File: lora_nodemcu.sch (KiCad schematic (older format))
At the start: 12 parts, among them U1 RFM95, U2 LM1117-3.3, U3 WeMos_mini

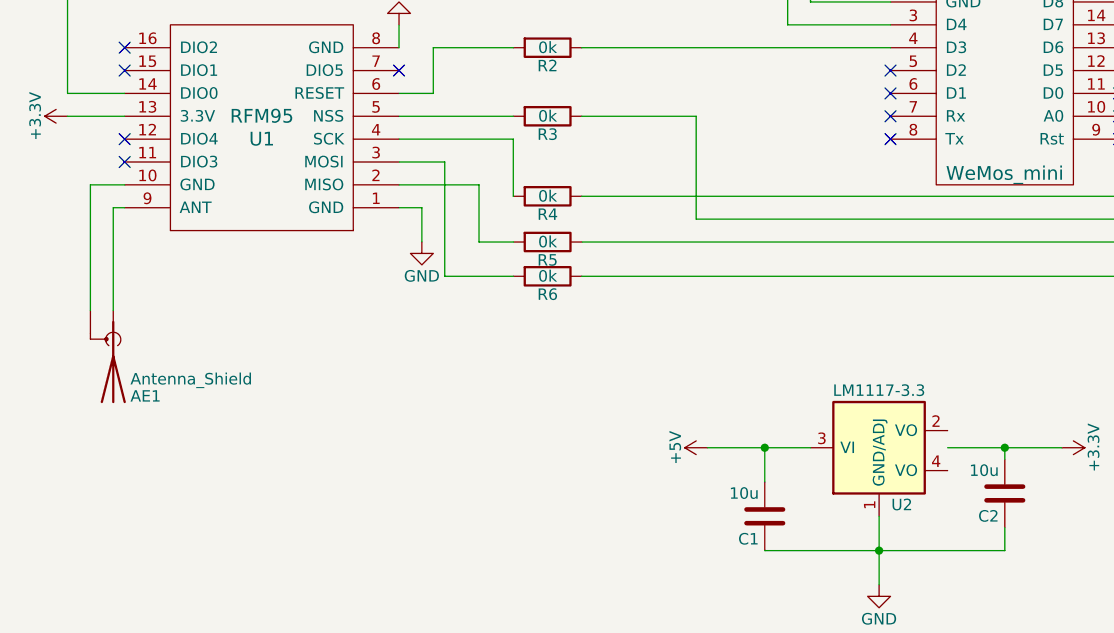
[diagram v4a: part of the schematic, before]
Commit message: fixed traces, added 3.3v power management
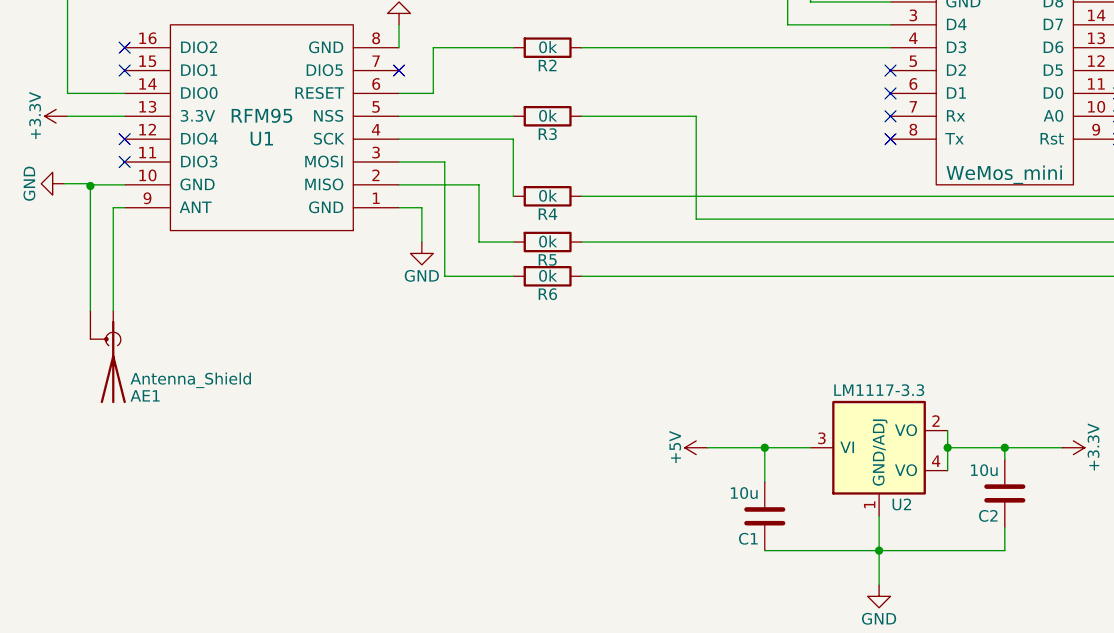
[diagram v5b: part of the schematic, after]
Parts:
- U2: footprint (none) -> TO_SOT_Packages_SMD:SOT-223
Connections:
- net +3V3: now also U2.2 (VO), U2.4 (VO)
- net GND: now also AE1.2 (Shield), U1.10 (GND)
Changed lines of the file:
@@
 LIBS:valves
 LIBS:rfm95
-LIBS:disaster_radio
 LIBS:lora_nodemcu-cache
 EELAYER 25 0
@@
 $EndComp
 $Comp
-L GND #PWR3
+L GND #PWR01
 U 1 1 59CB0D77
 P 5800 3650
-F 0 "#PWR3" H 5800 3400 50  0001 C CNN
+F 0 "#PWR01" H 5800 3400 50  0001 C CNN
 F 1 "GND" H 5800 3500 50  0000 C CNN
 F 2 "" H 5800 3650 50  0001 C CNN
@@
 $EndComp
 $Comp
-L GND #PWR2
+L GND #PWR02
 U 1 1 59CB0DA4
 P 5700 2700
-F 0 "#PWR2" H 5700 2450 50  0001 C CNN
+F 0 "#PWR02" H 5700 2450 50  0001 C CNN
 F 1 "GND" H 5700 2550 50  0000 C CNN
 F 2 "" H 5700 2700 50  0001 C CNN
@@
 $EndComp
 $Comp
-L +3.3V #PWR1
+L +3.3V #PWR03
 U 1 1 59CB1055
 P 4250 3100
-F 0 "#PWR1" H 4250 2950 50  0001 C CNN
+F 0 "#PWR03" H 4250 2950 50  0001 C CNN
 F 1 "+3.3V" H 4250 3240 50  0000 C CNN
 F 2 "" H 4250 3100 50  0001 C CNN
@@
 	0    1    1    0
 $EndComp
-Wire Wire Line
-	4500 3500 4450 3500
-Wire Wire Line
-	4450 3500 4450 3950
-Wire Wire Line
-	4500 3400 4350 3400
-Wire Wire Line
-	5700 3500 5800 3500
-Wire Wire Line
-	5800 3500 5800 3650
-Wire Wire Line
-	4500 3100 4250 3100
-Wire Wire Line
-	4350 3400 4350 3950
-Wire Wire Line
-	5900 3300 5700 3300
-Wire Wire Line
-	5700 3400 6050 3400
 $Comp
 L R R4
@@
 	0    1    1    0
 $EndComp
-Wire Wire Line
-	5700 3100 6200 3100
 $Comp
 L R R2
@@
 	0    1    1    0
 $EndComp
-Wire Wire Line
-	5850 3000 5700 3000
 $Comp
 L R R1
@@
 	0    1    1    0
 $EndComp
-Wire Wire Line
-	4500 3000 4250 3000
-$Comp
-L GND #PWR7
+$Comp
+L GND #PWR04
 U 1 1 59D2FC8A
 P 7800 5150
-F 0 "#PWR7" H 7800 4900 50  0001 C CNN
+F 0 "#PWR04" H 7800 4900 50  0001 C CNN
 F 1 "GND" H 7800 5000 50  0000 C CNN
 F 2 "" H 7800 5150 50  0001 C CNN
@@
 $EndComp
 $Comp
-L +3.3V #PWR8
+L +3.3V #PWR05
 U 1 1 59D2FCFE
 P 8600 4550
-F 0 "#PWR8" H 8600 4400 50  0001 C CNN
+F 0 "#PWR05" H 8600 4400 50  0001 C CNN
 F 1 "+3.3V" H 8600 4690 50  0000 C CNN
 F 2 "" H 8600 4550 50  0001 C CNN
@@
 $EndComp
 $Comp
-L +5V #PWR4
+L +5V #PWR06
 U 1 1 59D2FD9A
 P 7050 4550
-F 0 "#PWR4" H 7050 4400 50  0001 C CNN
+F 0 "#PWR06" H 7050 4400 50  0001 C CNN
 F 1 "+5V" H 7050 4690 50  0000 C CNN
 F 2 "" H 7050 4550 50  0001 C CNN
@@
 	0    -1   -1   0
 $EndComp
-Wire Wire Line
-	6050 3400 6050 3650
-Wire Wire Line
-	5700 3200 6200 3200
-Wire Wire Line
-	6200 3200 6200 3450
-Wire Wire Line
-	6200 2800 5850 2800
-Wire Wire Line
-	6200 2450 4250 2450
-Wire Wire Line
-	4250 2450 4250 3000
-Wire Wire Line
-	5700 2800 5700 2700
 $Comp
 L WeMos_mini U3
@@
 $EndComp
 $Comp
-L +5V #PWR6
+L +5V #PWR07
 U 1 1 59DAD071
 P 7700 2400
-F 0 "#PWR6" H 7700 2250 50  0001 C CNN
+F 0 "#PWR07" H 7700 2250 50  0001 C CNN
 F 1 "+5V" H 7700 2540 50  0000 C CNN
 F 2 "" H 7700 2400 50  0001 C CNN
@@
 $EndComp
 $Comp
-L GND #PWR5
+L GND #PWR08
 U 1 1 59DAD0A3
 P 7500 2400
-F 0 "#PWR5" H 7500 2150 50  0001 C CNN
+F 0 "#PWR08" H 7500 2150 50  0001 C CNN
 F 1 "GND" H 7500 2250 50  0000 C CNN
 F 2 "" H 7500 2400 50  0001 C CNN
@@
 $EndComp
 $Comp
-L +3.3V #PWR9
+L +3.3V #PWR09
 U 1 1 59DAD0D5
 P 9000 2400
-F 0 "#PWR9" H 9000 2250 50  0001 C CNN
+F 0 "#PWR09" H 9000 2250 50  0001 C CNN
 F 1 "+3.3V" H 9000 2540 50  0000 C CNN
 F 2 "" H 9000 2400 50  0001 C CNN
@@
 	1    0    0    -1
 $EndComp
-Wire Wire Line
-	9000 2400 9000 2500
-Wire Wire Line
-	9000 2500 8850 2500
-Wire Wire Line
-	7700 2400 7700 2500
-Wire Wire Line
-	7700 2500 7850 2500
-Wire Wire Line
-	7500 2400 7500 2600
-Wire Wire Line
-	7500 2600 7850 2600
-Wire Wire Line
-	8850 2600 9450 2600
-Wire Wire Line
-	7000 3550 9450 3550
-Wire Wire Line
-	7000 3100 6500 3100
 Text Label 8950 2600 0    60   ~ 0
 SS
-Wire Wire Line
-	8850 2700 9300 2700
-Wire Wire Line
-	9300 3800 6500 3800
 Text Label 8950 2700 0    60   ~ 0
 MOSI
 Text Label 8950 2800 0    60   ~ 0
 MISO
-Wire Wire Line
-	8850 2900 9100 2900
 Text Label 8950 2900 0    60   ~ 0
 SCK
-Wire Wire Line
-	6500 2800 7850 2800
-Wire Wire Line
-	7850 2700 7400 2700
-Wire Wire Line
-	7400 2700 7400 2450
-Wire Wire Line
-	7400 2450 6500 2450
 NoConn ~ 7850 2900
 NoConn ~ 7850 3000
@@
 NoConn ~ 8850 3100
 NoConn ~ 8850 3200
-Wire Wire Line
-	5900 3300 5900 3800
-Wire Wire Line
-	5900 3800 6200 3800
-Wire Wire Line
-	5850 2800 5850 3000
-Wire Wire Line
-	9300 2700 9300 3800
-Wire Wire Line
-	8850 2800 9200 2800
-Wire Wire Line
-	9200 2800 9200 3650
-Wire Wire Line
-	9100 2900 9100 3450
-Wire Wire Line
-	9100 3450 6500 3450
-Wire Wire Line
-	9200 3650 6500 3650
-Wire Wire Line
-	6050 3650 6200 3650
-Wire Wire Line
-	9450 3550 9450 2600
-Wire Wire Line
-	7000 3550 7000 3100
 NoConn ~ 4500 3200
 NoConn ~ 4500 3300
@@
 F 0 "U2" H 7900 4300 50  0000 C CNN
 F 1 "LM1117-3.3" H 7800 4800 50  0000 C CNN
-F 2 "" H 7800 4550 50  0001 C CNN
+F 2 "TO_SOT_Packages_SMD:SOT-223" H 7800 4550 50  0001 C CNN
 F 3 "" H 7800 4550 50  0001 C CNN
 	1    7800 4550
@@
 	-1   0    0    1
 $EndComp
+$Comp
+L GND #PWR?
+U 1 1 59E595E3
+P 4235 3395
+F 0 "#PWR?" H 4235 3145 50  0001 C CNN
+F 1 "GND" H 4235 3245 50  0000 C CNN
+F 2 "" H 4235 3395 50  0001 C CNN
+F 3 "" H 4235 3395 50  0001 C CNN
+	1    4235 3395
+	0    1    1    0
+$EndComp
+Wire Wire Line
+	4500 3500 4450 3500
+Wire Wire Line
+	4450 3500 4450 3950
+Wire Wire Line
+	4500 3400 4350 3400
+Wire Wire Line
+	5700 3500 5800 3500
+Wire Wire Line
+	5800 3500 5800 3650
+Wire Wire Line
+	4500 3100 4250 3100
+Wire Wire Line
+	4350 3400 4350 3950
+Wire Wire Line
+	5900 3300 5700 3300
+Wire Wire Line
+	5700 3400 6050 3400
+Wire Wire Line
+	5700 3100 6200 3100
+Wire Wire Line
+	5850 3000 5700 3000
+Wire Wire Line
+	4500 3000 4250 3000
+Wire Wire Line
+	6050 3400 6050 3650
+Wire Wire Line
+	5700 3200 6200 3200
+Wire Wire Line
+	6200 3200 6200 3450
+Wire Wire Line
+	6200 2800 5850 2800
+Wire Wire Line
+	6200 2450 4250 2450
+Wire Wire Line
+	4250 2450 4250 3000
+Wire Wire Line
+	5700 2800 5700 2700
+Wire Wire Line
+	9000 2400 9000 2500
+Wire Wire Line
+	9000 2500 8850 2500
+Wire Wire Line
+	7700 2400 7700 2500
+Wire Wire Line
+	7700 2500 7850 2500
+Wire Wire Line
+	7500 2400 7500 2600
+Wire Wire Line
+	7500 2600 7850 2600
+Wire Wire Line
+	8850 2600 9450 2600
+Wire Wire Line
+	7000 3550 9450 3550
+Wire Wire Line
+	7000 3100 6500 3100
+Wire Wire Line
+	8850 2700 9300 2700
+Wire Wire Line
+	9300 3800 6500 3800
+Wire Wire Line
+	8850 2900 9100 2900
+Wire Wire Line
+	6500 2800 7850 2800
+Wire Wire Line
+	7850 2700 7400 2700
+Wire Wire Line
+	7400 2700 7400 2450
+Wire Wire Line
+	7400 2450 6500 2450
+Wire Wire Line
+	5900 3300 5900 3800
+Wire Wire Line
+	5900 3800 6200 3800
+Wire Wire Line
+	5850 2800 5850 3000
+Wire Wire Line
+	9300 2700 9300 3800
+Wire Wire Line
+	8850 2800 9200 2800
+Wire Wire Line
+	9200 2800 9200 3650
+Wire Wire Line
+	9100 2900 9100 3450
+Wire Wire Line
+	9100 3450 6500 3450
+Wire Wire Line
+	9200 3650 6500 3650
+Wire Wire Line
+	6050 3650 6200 3650
+Wire Wire Line
+	9450 3550 9450 2600
+Wire Wire Line
+	7000 3550 7000 3100
 Wire Wire Line
 	8100 4550 8600 4550
@@
 	8350 5000 8350 4900
 Connection ~ 7800 5000
+Wire Wire Line
+	8100 4475 8100 4650
+Connection ~ 8100 4550
+Wire Wire Line
+	4350 3395 4350 3405
+Connection ~ 4350 3405
+Wire Wire Line
+	4235 3395 4350 3395
 $EndSCHEMATC

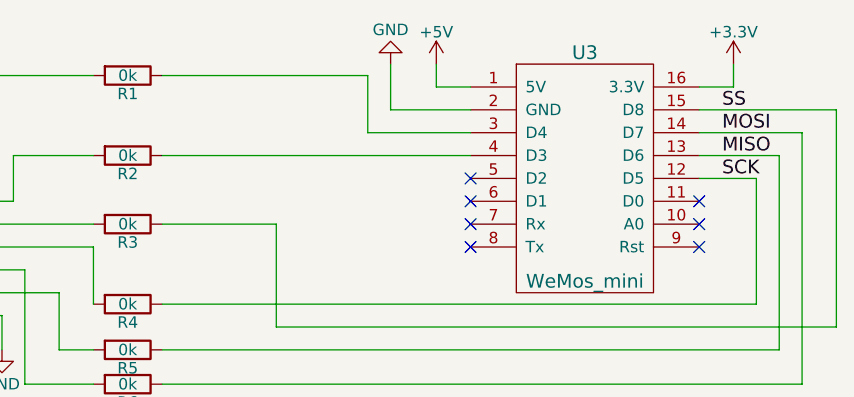
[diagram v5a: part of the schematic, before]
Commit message: Missing caps need to be added to voltage regulator.  Making a save to repo before pushing to Sudomesh repo.
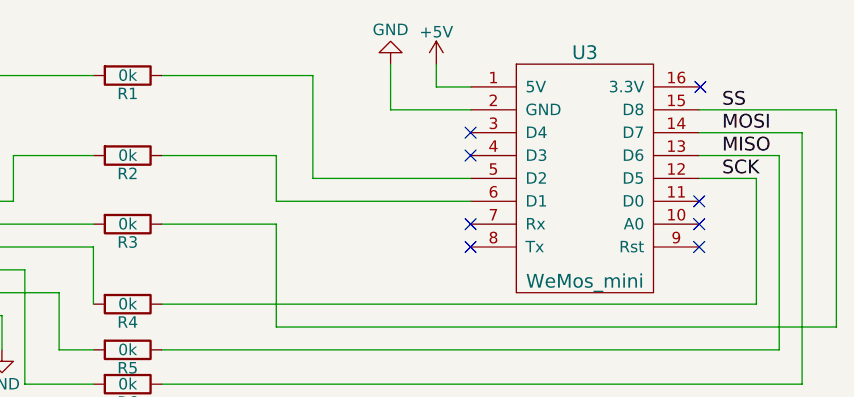
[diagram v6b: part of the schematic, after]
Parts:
- AE1: footprint Connectors:SMA_SMD_Jack_Straight -> Connectors_Molex:Molex_SMA_Jack_Edge_Mount
- C1, C2: footprint (none) -> Capacitors_SMD:C_0805_HandSoldering
- R1, R2, R3, R4, R5, R6: footprint Resistors_SMD:R_0805 -> Resistors_SMD:R_0805_HandSoldering
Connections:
- net +3V3: no longer U3.16 (3.3V)
- net at R2.1: now also U3.6 (D1); no longer U3.4 (D3)
- net at R1.1: now also U3.5 (D2); no longer U3.3 (D4)
- no-connect marks 12 -> 13
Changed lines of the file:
@@
 F 0 "AE1" H 4375 4325 50  0000 R CNN
 F 1 "Antenna_Shield" H 4375 4250 50  0000 R CNN
-F 2 "Connectors:SMA_SMD_Jack_Straight" H 4450 4250 50  0001 C CNN
+F 2 "Connectors_Molex:Molex_SMA_Jack_Edge_Mount" H 4450 4250 50  0001 C CNN
 F 3 "" H 4450 4250 50  0001 C CNN
 	1    4450 4150
@@
 F 0 "R3" V 6430 3100 50  0000 C CNN
 F 1 "0k" V 6350 3100 50  0000 C CNN
-F 2 "Resistors_SMD:R_0805" V 6280 3100 50  0001 C CNN
+F 2 "Resistors_SMD:R_0805_HandSoldering" V 6280 3100 50  0001 C CNN
 F 3 "" H 6350 3100 50  0001 C CNN
 	1    6350 3100
@@
 F 0 "R5" V 6430 3650 50  0000 C CNN
 F 1 "0k" V 6350 3650 50  0000 C CNN
-F 2 "Resistors_SMD:R_0805" V 6280 3650 50  0001 C CNN
+F 2 "Resistors_SMD:R_0805_HandSoldering" V 6280 3650 50  0001 C CNN
 F 3 "" H 6350 3650 50  0001 C CNN
 	1    6350 3650
@@
 F 0 "R6" V 6430 3800 50  0000 C CNN
 F 1 "0k" V 6350 3800 50  0000 C CNN
-F 2 "Resistors_SMD:R_0805" V 6280 3800 50  0001 C CNN
+F 2 "Resistors_SMD:R_0805_HandSoldering" V 6280 3800 50  0001 C CNN
 F 3 "" H 6350 3800 50  0001 C CNN
 	1    6350 3800
@@
 F 0 "R4" V 6430 3450 50  0000 C CNN
 F 1 "0k" V 6350 3450 50  0000 C CNN
-F 2 "Resistors_SMD:R_0805" V 6280 3450 50  0001 C CNN
+F 2 "Resistors_SMD:R_0805_HandSoldering" V 6280 3450 50  0001 C CNN
 F 3 "" H 6350 3450 50  0001 C CNN
 	1    6350 3450
@@
 F 0 "R2" V 6430 2800 50  0000 C CNN
 F 1 "0k" V 6350 2800 50  0000 C CNN
-F 2 "Resistors_SMD:R_0805" V 6280 2800 50  0001 C CNN
+F 2 "Resistors_SMD:R_0805_HandSoldering" V 6280 2800 50  0001 C CNN
 F 3 "" H 6350 2800 50  0001 C CNN
 	1    6350 2800
@@
 F 0 "R1" V 6430 2450 50  0000 C CNN
 F 1 "0k" V 6350 2450 50  0000 C CNN
-F 2 "Resistors_SMD:R_0805" V 6280 2450 50  0001 C CNN
+F 2 "Resistors_SMD:R_0805_HandSoldering" V 6280 2450 50  0001 C CNN
 F 3 "" H 6350 2450 50  0001 C CNN
 	1    6350 2450
@@
 	-1   0    0    1
 $EndComp
-$Comp
-L +3.3V #PWR09
-U 1 1 59DAD0D5
-P 9000 2400
-F 0 "#PWR09" H 9000 2250 50  0001 C CNN
-F 1 "+3.3V" H 9000 2540 50  0000 C CNN
-F 2 "" H 9000 2400 50  0001 C CNN
-F 3 "" H 9000 2400 50  0001 C CNN
-	1    9000 2400
-	1    0    0    -1
-$EndComp
 Text Label 8950 2600 0    60   ~ 0
 SS
@@
 Text Label 8950 2900 0    60   ~ 0
 SCK
-NoConn ~ 7850 2900
-NoConn ~ 7850 3000
 NoConn ~ 7850 3100
 NoConn ~ 7850 3200
@@
 F 0 "C2" H 8375 4850 50  0000 L CNN
 F 1 "10u" H 8375 4650 50  0000 L CNN
-F 2 "" H 8388 4600 50  0001 C CNN
+F 2 "Capacitors_SMD:C_0805_HandSoldering" H 8388 4600 50  0001 C CNN
 F 3 "" H 8350 4750 50  0001 C CNN
 	1    8350 4750
@@
 F 0 "C1" H 7325 4950 50  0000 L CNN
 F 1 "10u" H 7325 4750 50  0000 L CNN
-F 2 "" H 7338 4700 50  0001 C CNN
+F 2 "Capacitors_SMD:C_0805_HandSoldering" H 7338 4700 50  0001 C CNN
 F 3 "" H 7300 4850 50  0001 C CNN
 	1    7300 4850
@@
 $EndComp
 $Comp
-L GND #PWR?
+L GND #PWR09
 U 1 1 59E595E3
 P 4235 3395
-F 0 "#PWR?" H 4235 3145 50  0001 C CNN
+F 0 "#PWR09" H 4235 3145 50  0001 C CNN
 F 1 "GND" H 4235 3245 50  0000 C CNN
 F 2 "" H 4235 3395 50  0001 C CNN
@@
 	5700 2800 5700 2700
 Wire Wire Line
-	9000 2400 9000 2500
-Wire Wire Line
-	9000 2500 8850 2500
-Wire Wire Line
 	7700 2400 7700 2500
 Wire Wire Line
@@
 Wire Wire Line
 	8850 2900 9100 2900
-Wire Wire Line
-	6500 2800 7850 2800
-Wire Wire Line
-	7850 2700 7400 2700
-Wire Wire Line
-	7400 2700 7400 2450
-Wire Wire Line
-	7400 2450 6500 2450
 Wire Wire Line
 	5900 3300 5900 3800
@@
 Wire Wire Line
 	4235 3395 4350 3395
+NoConn ~ 7850 2800
+NoConn ~ 8855 2500
+Wire Wire Line
+	7160 2450 6500 2450
+Wire Wire Line
+	7850 3000 7000 3000
+Wire Wire Line
+	7000 3000 7000 2800
+Wire Wire Line
+	7000 2800 6500 2800
+Wire Wire Line
+	7160 2450 7160 2900
+Wire Wire Line
+	7160 2900 7850 2900
+NoConn ~ 7850 2700
 $EndSCHEMATC

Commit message: Saving changes to circuit board prior to reworking yet again.
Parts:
- AE1: symbol Antenna_Shield -> device:Antenna_Shield
- C1, C2: symbol C -> device:C
- R1, R2, R3, R4, R5, R6: symbol R -> device:R
- U1: symbol RFM95 -> rfm95:RFM95
- U2: symbol LM1117-3.3 -> lora_nodemcu-rescue:LM1117-3.3-RESCUE-lora_nodemcu
- U3: footprint DisasterRadio:D1_mini_Hat -> DisasterRadio:D1_mini_board; symbol WeMos_mini -> lora_nodemcu-rescue:WeMos_mini-RESCUE-lora_nodemcu
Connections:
- net GND: no longer U1.10 (GND)
- net 50Ohm: now reaches AE1.1 (A), U1.9 (ANT)
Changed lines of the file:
@@
-EESchema Schematic File Version 2
-LIBS:power
-LIBS:device
-LIBS:transistors
-LIBS:conn
-LIBS:linear
-LIBS:regul
-LIBS:74xx
-LIBS:cmos4000
-LIBS:adc-dac
-LIBS:memory
-LIBS:xilinx
-LIBS:microcontrollers
-LIBS:dsp
-LIBS:microchip
-LIBS:analog_switches
-LIBS:motorola
-LIBS:texas
-LIBS:intel
-LIBS:audio
-LIBS:interface
-LIBS:digital-audio
-LIBS:philips
-LIBS:display
-LIBS:cypress
-LIBS:siliconi
-LIBS:opto
-LIBS:atmel
-LIBS:contrib
-LIBS:valves
-LIBS:rfm95
+EESchema Schematic File Version 4
 LIBS:lora_nodemcu-cache
-EELAYER 25 0
+EELAYER 26 0
 EELAYER END
 $Descr A4 11693 8268
@@
 $EndDescr
 $Comp
-L RFM95 U1
+L rfm95:RFM95 U1
 U 1 1 59C9C638
 P 5150 3150
@@
 $EndComp
 $Comp
-L Antenna_Shield AE1
+L device:Antenna_Shield AE1
 U 1 1 59CB0BD9
 P 4450 4150
@@
 $EndComp
 $Comp
-L GND #PWR01
+L power:GND #PWR01
 U 1 1 59CB0D77
 P 5800 3650
@@
 $EndComp
 $Comp
-L GND #PWR02
+L power:GND #PWR02
 U 1 1 59CB0DA4
 P 5700 2700
@@
 $EndComp
 $Comp
-L +3.3V #PWR03
+L power:+3.3V #PWR03
 U 1 1 59CB1055
 P 4250 3100
@@
 $EndComp
 $Comp
-L R R3
+L device:R R3
 U 1 1 59CC447A
 P 6350 3100
@@
 $EndComp
 $Comp
-L R R5
+L device:R R5
 U 1 1 59CC4726
 P 6350 3650
@@
 $EndComp
 $Comp
-L R R6
+L device:R R6
 U 1 1 59CC47A1
 P 6350 3800
@@
 $EndComp
 $Comp
-L R R4
+L device:R R4
 U 1 1 59CF0F92
 P 6350 3450
@@
 $EndComp
 $Comp
-L R R2
+L device:R R2
 U 1 1 59CF1001
 P 6350 2800
@@
 $EndComp
 $Comp
-L R R1
+L device:R R1
 U 1 1 59CF1A56
 P 6350 2450
@@
 $EndComp
 $Comp
-L GND #PWR04
+L power:GND #PWR04
 U 1 1 59D2FC8A
 P 7800 5150
@@
 $EndComp
 $Comp
-L +3.3V #PWR05
+L power:+3.3V #PWR05
 U 1 1 59D2FCFE
 P 8600 4550
@@
 $EndComp
 $Comp
-L +5V #PWR06
+L power:+5V #PWR06
 U 1 1 59D2FD9A
 P 7050 4550
@@
 $EndComp
 $Comp
-L WeMos_mini U3
+L lora_nodemcu-rescue:WeMos_mini-RESCUE-lora_nodemcu U3
 U 1 1 59DACFEC
 P 8350 2850
 F 0 "U3" H 8350 3350 60  0000 C CNN
 F 1 "WeMos_mini" H 8350 2350 60  0000 C CNN
-F 2 "DisasterRadio:D1_mini_Hat" H 8900 2150 60  0001 C CNN
+F 2 "DisasterRadio:D1_mini_board" H 8900 2150 60  0001 C CNN
 F 3 "" H 8900 2150 60  0000 C CNN
 	1    8350 2850
@@
 $EndComp
 $Comp
-L +5V #PWR07
+L power:+5V #PWR07
 U 1 1 59DAD071
 P 7700 2400
@@
 $EndComp
 $Comp
-L GND #PWR08
+L power:GND #PWR08
 U 1 1 59DAD0A3
 P 7500 2400
@@
 NoConn ~ 4500 2800
 $Comp
-L LM1117-3.3 U2
+L lora_nodemcu-rescue:LM1117-3.3-RESCUE-lora_nodemcu U2
 U 1 1 59DDA3AE
 P 7800 4550
@@
 $EndComp
 $Comp
-L C C2
+L device:C C2
 U 1 1 59DDA417
 P 8350 4750
@@
 $EndComp
 $Comp
-L C C1
+L device:C C1
 U 1 1 59DDA458
 P 7300 4850
@@
 $EndComp
 $Comp
-L GND #PWR09
+L power:GND #PWR09
 U 1 1 59E595E3
 P 4235 3395
@@
 	4500 3100 4250 3100
 Wire Wire Line
-	4350 3400 4350 3950
+	4350 3395 4350 3950
 Wire Wire Line
 	5900 3300 5700 3300
@@
 	8100 4475 8100 4650
 Connection ~ 8100 4550
-Wire Wire Line
-	4350 3395 4350 3405
 Connection ~ 4350 3405
 Wire Wire Line
@@
 	7160 2900 7850 2900
 NoConn ~ 7850 2700
+Text Label 4450 3720 0    60   ~ 0
+50Ohm
 $EndSCHEMATC
